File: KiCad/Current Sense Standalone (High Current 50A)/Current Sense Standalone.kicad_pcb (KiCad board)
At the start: 2 copper layers, 62.3 x 24.3 mm, 9 parts, among them J1 PLUG INPUT BATTERY IN HERE (X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, J3 V+/- TEST Header PIN, J6 to MCU GPIO PIN, J7 PLUG BATTERY OUTPUT HERE (XT6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, U1 INA139QPWRQ1

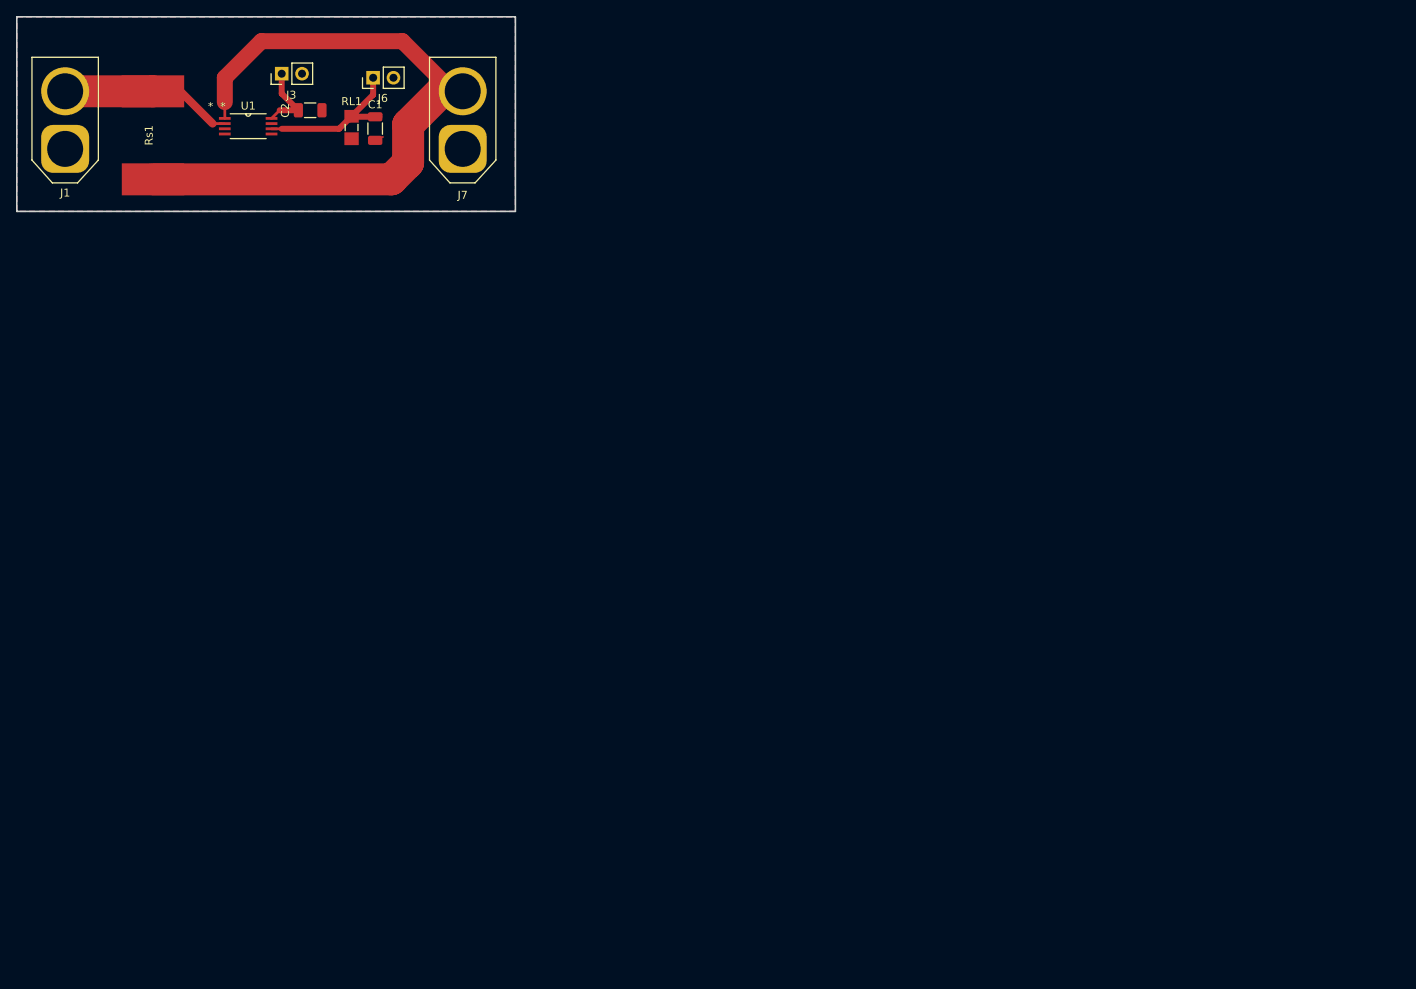
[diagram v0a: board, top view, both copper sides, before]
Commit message: Current Sense Dimensions
Adjusted dimensions of the width and length of the board. Still in-progress with the components.
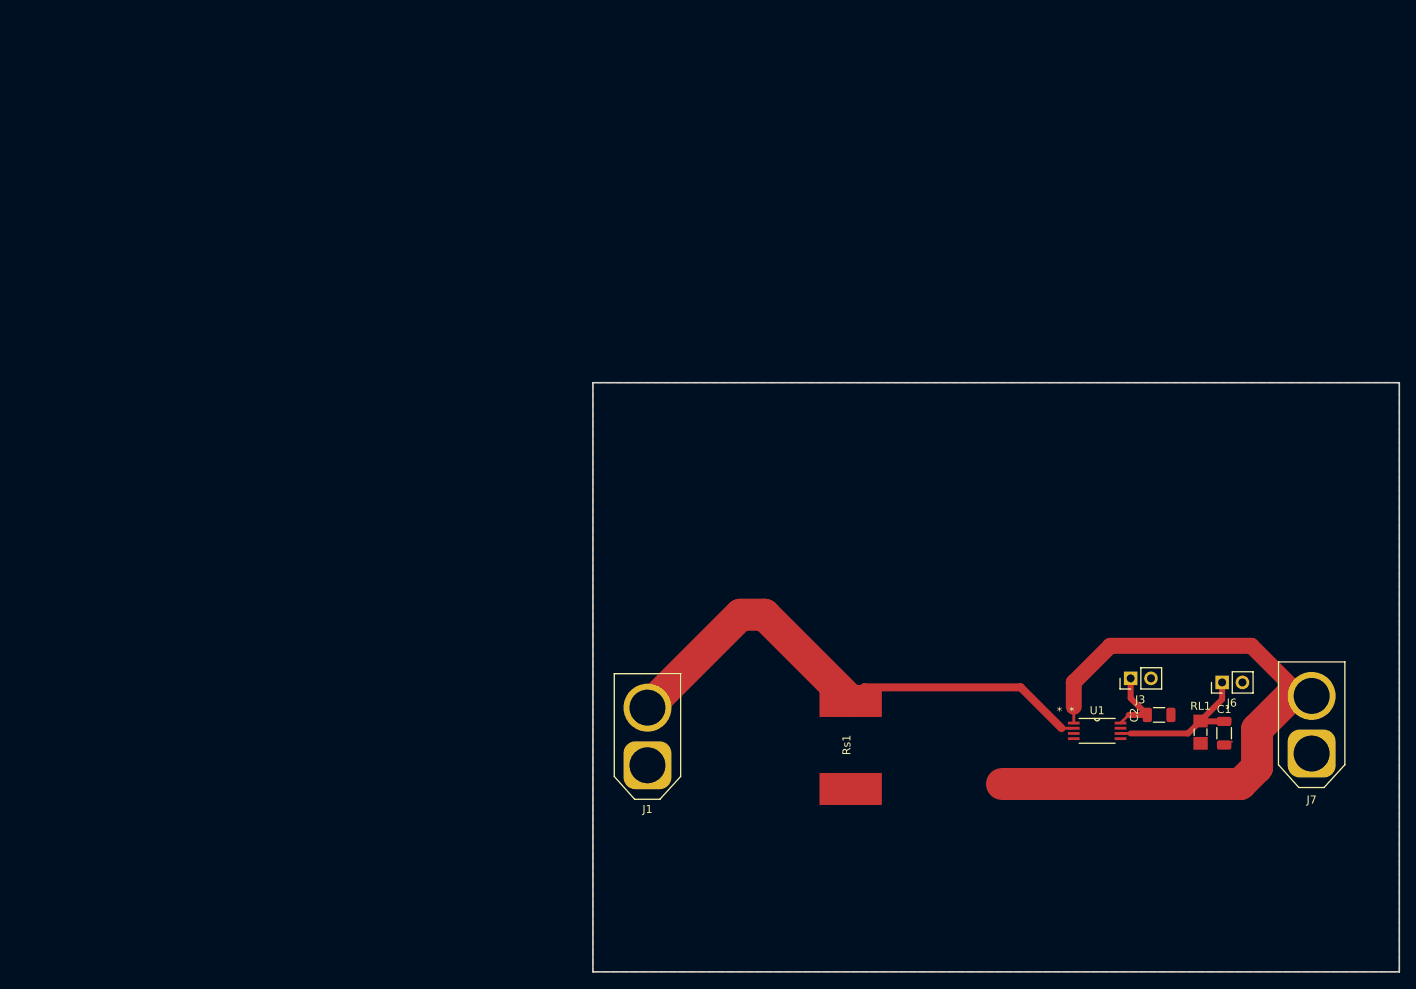
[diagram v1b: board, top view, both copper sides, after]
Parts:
- moved J3 130.3 mm to (151.8, 95.4)
- moved J6 130.3 mm to (163.3, 95.9)
- moved J7 130.3 mm to (174.5, 104.8)
- moved RL1 130.3 mm to (160.6, 102.1)
- moved C1 130.3 mm to (163.5, 102.3)
- moved C2 130.3 mm to (155.4, 100.0)
- moved U1 130.3 mm to (147.6, 102.0)
- moved Rs1 115.8 mm to (116.8, 103.7)
- moved J1 106.0 mm to (91.4, 106.3)
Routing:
- net /Batt+: track 27.3 -> 65.4 mm
- net GND: track 3.51 -> 0.88 mm
- removed copper zone on B.Cu, net GND
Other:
- board size 62.3 x 24.3 mm -> 100.8 x 73.6 mm

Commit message: Update Current Sense Standalone.kicad_pcb
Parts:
- moved J3 32.8 mm to (137.2, 66.0)
- moved J6 22.3 mm to (162.6, 73.7)
- moved U1 18.8 mm to (137.2, 86.4)
- moved Rs1 9.66 mm to (114.3, 94.4)
- moved J1 8.68 mm to (91.4, 97.6)
- moved J7 7.21 mm to (174.5, 97.6)
- moved C2 5.77 mm to (149.9, 101.6)
- moved RL1 3.14 mm to (157.5, 101.6)
- moved C1 0.65 mm to (163.5, 101.6)
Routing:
- net /Batt-: track 84.1 -> 0.00 mm
- net /Batt+: track 65.4 -> 0.00 mm
- net /Vout: track 21.1 -> 0.00 mm
- net /V-: track 9.21 -> 0.00 mm
- net GND: track 0.88 -> 0.00 mm
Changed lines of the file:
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@@
   (net 8 "/Batt-")
   (footprint "Mechatronic Footprints:AMASS_XT60-F_1x02_P7.20mm_Vertical" (layer "F.Cu")
-    (at 174.464045 104.790486 90)
+    (at 174.464045 97.58 90)
     (descr "AMASS female XT60, through hole, vertical, https://www.tme.eu/Document/2d152ced3b7a446066e6c419d84bb460/XT60%20SPEC.pdf")
     (tags "XT60 female vertical")
@@
   )
   (footprint "Capacitor_SMD:C_1206_3216Metric" (layer "F.Cu")
-    (at 155.396 99.964486)
+    (at 149.86 101.6)
     (descr "Capacitor SMD 1206 (3216 Metric), square (rectangular) end terminal, IPC_7351 nominal, (Body size source: IPC-SM-782 page 76, https://www.pcb-3d.com/wordpress/wp-content/uploads/ipc-sm-782a_amendment_1_and_2.pdf), generated with kicad-footprint-generator")
     (tags "capacitor")
@@
   )
   (footprint "RC1206FR-13100KL:RESC3216X65" (layer "F.Cu")
-    (at 160.573375 102.120486 -90)
+    (at 157.48 101.6 -90)
     (descr "<b>RESISTOR</b>")
     (property "Sheetfile" "Current Sense Standalone.kicad_sch")
@@
   )
   (footprint "Mechatronic Footprints:CSS2H-5930R" (layer "F.Cu")
-    (at 116.84 103.72 90)
+    (at 114.3 94.4 90)
     (property "Sheetfile" "Current Sense Standalone.kicad_sch")
     (property "Sheetname" "")
@@
   )
   (footprint "Capacitor_SMD:C_1206_3216Metric" (layer "F.Cu")
-    (at 163.524 102.250486 -90)
+    (at 163.524 101.6 -90)
     (descr "Capacitor SMD 1206 (3216 Metric), square (rectangular) end terminal, IPC_7351 nominal, (Body size source: IPC-SM-782 page 76, https://www.pcb-3d.com/wordpress/wp-content/uploads/ipc-sm-782a_amendment_1_and_2.pdf), generated with kicad-footprint-generator")
     (tags "capacitor")
@@
   )
   (footprint "Connector_PinHeader_2.54mm:PinHeader_1x02_P2.54mm_Vertical" (layer "F.Cu")
-    (at 151.84 95.392486 90)
+    (at 137.16 66.04 90)
     (descr "Through hole straight pin header, 1x02, 2.54mm pitch, single row")
     (tags "Through hole pin header THT 1x02 2.54mm single row")
@@
   )
   (footprint "Mechatronic Footprints:INA139_PW8" (layer "F.Cu")
-    (at 147.649 101.955485)
+    (at 137.16 86.36)
     (tags "INA139QPWRQ1 ")
     (property "Sheetfile" "Current Sense Standalone.kicad_sch")
@@
   )
   (footprint "Mechatronic Footprints:AMASS_XT60-M_1x02_P7.20mm_Vertical" (layer "F.Cu")
-    (at 91.44 106.26 90)
+    (at 91.44 97.58 90)
     (descr "AMASS female XT60, through hole, vertical, https://www.tme.eu/Document/2d152ced3b7a446066e6c419d84bb460/XT60%20SPEC.pdf")
     (tags "XT60 female vertical")
@@
   )
   (footprint "Connector_PinHeader_2.54mm:PinHeader_1x02_P2.54mm_Vertical" (layer "F.Cu")
-    (at 163.27 95.900486 90)
+    (at 162.56 73.66 90)
     (descr "Through hole straight pin header, 1x02, 2.54mm pitch, single row")
     (tags "Through hole pin header THT 1x02 2.54mm single row")
@@
   (gr_rect (start 84.62 58.44) (end 185.42 132.08)
     (stroke (width 0.2) (type default)) (fill none) (layer "Edge.Cuts"))
-  (segment (start 163.27 95.900486) (end 163.27 98.023861) (width 0.75) (layer "F.Cu") (net 1))
-  (segment (start 163.27 98.023861) (end 160.783751 100.51011) (width 0.75) (layer "F.Cu") (net 1))
-  (segment (start 160.783751 100.51011) (end 160.573375 100.51011) (width 0.25) (layer "F.Cu") (net 1))
-  (segment (start 164.062862 100.775486) (end 164.328238 100.51011) (width 0.25) (layer "F.Cu") (net 1))
-  (segment (start 160.838751 100.775486) (end 164.062862 100.775486) (width 0.75) (layer "F.Cu") (net 1))
-  (segment (start 150.57 102.280486) (end 151.84 102.280486) (width 0.35) (layer "F.Cu") (net 1))
-  (segment (start 151.84 102.280486) (end 159.013375 102.280486) (width 0.75) (layer "F.Cu") (net 1))
-  (segment (start 159.013375 102.280486) (end 160.573375 100.720486) (width 0.75) (layer "F.Cu") (net 1))
-  (segment (start 160.102999 100.980486) (end 160.573375 100.51011) (width 0.25) (layer "F.Cu") (net 1))
-  (segment (start 160.573375 100.51011) (end 160.838751 100.775486) (width 0.25) (layer "F.Cu") (net 1))
-  (segment (start 164.483078 103.30527) (end 164.478238 103.31011) (width 0.25) (layer "F.Cu") (net 2))
-  (segment (start 160.783751 103.31011) (end 160.163375 103.930486) (width 0.25) (layer "F.Cu") (net 2))
-  (segment (start 150.57 100.980486) (end 151.586 99.964486) (width 0.35) (layer "F.Cu") (net 3))
-  (segment (start 151.84 97.883486) (end 151.84 95.392486) (width 0.75) (layer "F.Cu") (net 3))
-  (segment (start 153.921 99.964486) (end 151.84 97.883486) (width 0.75) (layer "F.Cu") (net 3))
-  (segment (start 151.586 99.964486) (end 153.921 99.964486) (width 0.75) (layer "F.Cu") (net 3))
-  (segment (start 118.54 96.52) (end 138.093516 96.52) (width 1) (layer "F.Cu") (net 7))
-  (segment (start 144.22 101.630484) (end 144.728 101.630484) (width 0.25) (layer "F.Cu") (net 7))
-  (segment (start 103.061503 87.438497) (end 91.44 99.06) (width 4) (layer "F.Cu") (net 7))
-  (segment (start 143.204 101.630484) (end 144.22 101.630484) (width 0.35) (layer "F.Cu") (net 7))
-  (segment (start 138.093516 96.52) (end 143.204 101.630484) (width 1) (layer "F.Cu") (net 7))
-  (segment (start 116.84 98.22) (end 118.54 96.52) (width 1) (layer "F.Cu") (net 7))
-  (segment (start 116.84 98.22) (end 106.058497 87.438497) (width 4) (layer "F.Cu") (net 7))
-  (segment (start 106.058497 87.438497) (end 103.061503 87.438497) (width 4) (layer "F.Cu") (net 7))
-  (segment (start 171.813027 97.590486) (end 174.464045 97.590486) (width 4) (layer "F.Cu") (net 8))
-  (segment (start 167.64 101.763513) (end 171.813027 97.590486) (width 4) (layer "F.Cu") (net 8))
-  (segment (start 144.728 95.900486) (end 149.3 91.328486) (width 2) (layer "F.Cu") (net 8))
-  (segment (start 166.932045 91.328486) (end 173.194045 97.590486) (width 2) (layer "F.Cu") (net 8))
-  (segment (start 144.728 98.948486) (end 144.728 100.980486) (width 0.35) (layer "F.Cu") (net 8))
-  (segment (start 135.749273 108.598497) (end 135.751262 108.600486) (width 2) (layer "F.Cu") (net 8))
-  (segment (start 165.556 108.600486) (end 167.64 106.516486) (width 4) (layer "F.Cu") (net 8))
-  (segment (start 135.751262 108.600486) (end 165.556 108.600486) (width 4) (layer "F.Cu") (net 8))
-  (segment (start 144.728 98.948486) (end 144.728 95.900486) (width 2) (layer "F.Cu") (net 8))
-  (segment (start 149.3 91.328486) (end 166.932045 91.328486) (width 2) (layer "F.Cu") (net 8))
-  (segment (start 167.64 106.516486) (end 167.64 101.763513) (width 4) (layer "F.Cu") (net 8))
   (zone (net 2) (net_name "GND") (layer "F.Cu") (hatch edge 0.5)
     (connect_pads (clearance 0.5))

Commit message: Resume Builder - Jaxon
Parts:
- moved J3 48.9 mm to (160.0, 109.2)
- moved J6 39.8 mm to (144.8, 109.2)
- moved C2 23.1 mm to (162.6, 120.9), turned to -90 degrees
- moved C1 21.0 mm to (155.0, 120.8)
- moved RL1 21.0 mm to (149.0, 120.8)
- moved Rs1 20.1 mm to (132.7, 86.4), turned to 180 degrees
- moved J7 19.9 mm to (154.6, 97.5)
- moved J1 16.6 mm to (108.0, 97.4)
- moved U1 13.0 mm to (134.2, 99.1)
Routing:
- net /V-: track 0.00 -> 38.7 mm
- net /Vout: track 0.00 -> 31.5 mm
- net /Batt+: track 0.00 -> 14.6 mm
- net /Batt-: track 0.00 -> 14.6 mm
- added copper zone on F.Cu, net /Batt+
- added copper zone on F.Cu, net /Batt-
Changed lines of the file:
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@@
   (net 8 "/Batt-")
   (footprint "Mechatronic Footprints:AMASS_XT60-F_1x02_P7.20mm_Vertical" (layer "F.Cu")
-    (at 174.464045 97.58 90)
+    (at 154.558994 97.461689 90)
     (descr "AMASS female XT60, through hole, vertical, https://www.tme.eu/Document/2d152ced3b7a446066e6c419d84bb460/XT60%20SPEC.pdf")
     (tags "XT60 female vertical")
@@
   )
   (footprint "Capacitor_SMD:C_1206_3216Metric" (layer "F.Cu")
-    (at 149.86 101.6)
+    (at 162.56 120.855 -90)
     (descr "Capacitor SMD 1206 (3216 Metric), square (rectangular) end terminal, IPC_7351 nominal, (Body size source: IPC-SM-782 page 76, https://www.pcb-3d.com/wordpress/wp-content/uploads/ipc-sm-782a_amendment_1_and_2.pdf), generated with kicad-footprint-generator")
     (tags "capacitor")
@@
     (property "ki_keywords" "capacitor cap")
     (attr smd)
-    (fp_text reference "C2" (at -3.112128 0.016213 90) (layer "F.SilkS")
-        (effects (font (size 1 1) (thickness 0.15)))
-    )
-    (fp_text value "0.1uF" (at 3.158882 0.112988 90) (layer "F.Fab")
-        (effects (font (size 1 1) (thickness 0.15)))
-    )
-    (fp_text user "${REFERENCE}" (at 0 0) (layer "F.Fab")
+    (fp_text reference "C2" (at -3.112128 0.016213) (layer "F.SilkS")
+        (effects (font (size 1 1) (thickness 0.15)))
+    )
+    (fp_text value "0.1uF" (at 3.158882 0.112988) (layer "F.Fab")
+        (effects (font (size 1 1) (thickness 0.15)))
+    )
+    (fp_text user "${REFERENCE}" (at 0 0 90) (layer "F.Fab")
         (effects (font (size 0.8 0.8) (thickness 0.12)))
     )
@@
     (fp_line (start 1.6 0.8) (end -1.6 0.8)
       (stroke (width 0.1) (type solid)) (layer "F.Fab"))
-    (pad "1" smd roundrect (at -1.475 0) (size 1.15 1.8) (layers "F.Cu" "F.Paste" "F.Mask") (roundrect_rratio 0.2173913043)
+    (pad "1" smd roundrect (at -1.475 0 270) (size 1.15 1.8) (layers "F.Cu" "F.Paste" "F.Mask") (roundrect_rratio 0.2173913043)
       (net 3 "/V-") (pintype "passive"))
-    (pad "2" smd roundrect (at 1.475 0) (size 1.15 1.8) (layers "F.Cu" "F.Paste" "F.Mask") (roundrect_rratio 0.2173913043)
+    (pad "2" smd roundrect (at 1.475 0 270) (size 1.15 1.8) (layers "F.Cu" "F.Paste" "F.Mask") (roundrect_rratio 0.2173913043)
       (net 2 "GND") (pintype "passive"))
     (model "${KICAD6_3DMODEL_DIR}/Capacitor_SMD.3dshapes/C_1206_3216Metric.wrl"
@@
   )
   (footprint "RC1206FR-13100KL:RESC3216X65" (layer "F.Cu")
-    (at 157.48 101.6 -90)
+    (at 148.971 120.78 -90)
     (descr "<b>RESISTOR</b>")
     (property "Sheetfile" "Current Sense Standalone.kicad_sch")
@@
   )
   (footprint "Mechatronic Footprints:CSS2H-5930R" (layer "F.Cu")
-    (at 114.3 94.4 90)
+    (at 132.72 86.36 180)
     (property "Sheetfile" "Current Sense Standalone.kicad_sch")
     (property "Sheetname" "")
@@
     (property "ki_keywords" "r resistor")
     (attr smd)
-    (fp_text reference "Rs1" (at 0 -0.5 90 unlocked) (layer "F.SilkS")
-        (effects (font (size 1 1) (thickness 0.15)))
-    )
-    (fp_text value "R_Small_US" (at 0 -5.08 90 unlocked) (layer "F.Fab")
-        (effects (font (size 1 1) (thickness 0.15)))
-    )
-    (fp_text user "${REFERENCE}" (at 0 4.953 90 unlocked) (layer "F.Fab")
-        (effects (font (size 1 1) (thickness 0.15)))
-    )
-    (pad "1" smd rect (at -5.5 0 180) (size 7.8 4) (layers "F.Cu" "F.Paste" "F.Mask")
+    (fp_text reference "Rs1" (at 0 -0.5 unlocked) (layer "F.SilkS")
+        (effects (font (size 1 1) (thickness 0.15)))
+    )
+    (fp_text value "R_Small_US" (at 0 -5.08 unlocked) (layer "F.Fab")
+        (effects (font (size 1 1) (thickness 0.15)))
+    )
+    (fp_text user "${REFERENCE}" (at 0 4.953 unlocked) (layer "F.Fab")
+        (effects (font (size 1 1) (thickness 0.15)))
+    )
+    (pad "1" smd rect (at -5.5 0 270) (size 7.8 4) (layers "F.Cu" "F.Paste" "F.Mask")
       (net 8 "/Batt-") (pintype "passive") (thermal_bridge_angle 45))
-    (pad "2" smd rect (at 5.5 0 180) (size 7.8 4) (layers "F.Cu" "F.Paste" "F.Mask")
+    (pad "2" smd rect (at 5.5 0 270) (size 7.8 4) (layers "F.Cu" "F.Paste" "F.Mask")
       (net 7 "/Batt+") (pintype "passive") (thermal_bridge_angle 45))
   )
   (footprint "Capacitor_SMD:C_1206_3216Metric" (layer "F.Cu")
-    (at 163.524 101.6 -90)
+    (at 155.015 120.78 -90)
     (descr "Capacitor SMD 1206 (3216 Metric), square (rectangular) end terminal, IPC_7351 nominal, (Body size source: IPC-SM-782 page 76, https://www.pcb-3d.com/wordpress/wp-content/uploads/ipc-sm-782a_amendment_1_and_2.pdf), generated with kicad-footprint-generator")
     (tags "capacitor")
@@
   )
   (footprint "Connector_PinHeader_2.54mm:PinHeader_1x02_P2.54mm_Vertical" (layer "F.Cu")
-    (at 137.16 66.04 90)
+    (at 160.02 109.22 90)
     (descr "Through hole straight pin header, 1x02, 2.54mm pitch, single row")
     (tags "Through hole pin header THT 1x02 2.54mm single row")
@@
   )
   (footprint "Mechatronic Footprints:INA139_PW8" (layer "F.Cu")
-    (at 137.16 86.36)
+    (at 134.239 99.06)
     (tags "INA139QPWRQ1 ")
     (property "Sheetfile" "Current Sense Standalone.kicad_sch")
@@
   )
   (footprint "Mechatronic Footprints:AMASS_XT60-M_1x02_P7.20mm_Vertical" (layer "F.Cu")
-    (at 91.44 97.58 90)
+    (at 108.024461 97.415276 90)
     (descr "AMASS female XT60, through hole, vertical, https://www.tme.eu/Document/2d152ced3b7a446066e6c419d84bb460/XT60%20SPEC.pdf")
     (tags "XT60 female vertical")
@@
   )
   (footprint "Connector_PinHeader_2.54mm:PinHeader_1x02_P2.54mm_Vertical" (layer "F.Cu")
-    (at 162.56 73.66 90)
+    (at 144.78 109.22 90)
     (descr "Through hole straight pin header, 1x02, 2.54mm pitch, single row")
     (tags "Through hole pin header THT 1x02 2.54mm single row")
@@
   (gr_rect (start 84.62 58.44) (end 185.42 132.08)
     (stroke (width 0.2) (type default)) (fill none) (layer "Edge.Cuts"))
+  (segment (start 144.78 109.22) (end 144.78 115.189) (width 0.25) (layer "F.Cu") (net 1))
+  (segment (start 144.78 109.22) (end 144.78 106.090599) (width 0.25) (layer "F.Cu") (net 1))
+  (segment (start 144.78 106.090599) (end 138.074402 99.385001) (width 0.25) (layer "F.Cu") (net 1))
+  (segment (start 138.074402 99.385001) (end 137.16 99.385001) (width 0.25) (layer "F.Cu") (net 1))
+  (segment (start 144.78 115.189) (end 148.971 119.38) (width 0.25) (layer "F.Cu") (net 1))
+  (segment (start 155.015 119.305) (end 154.94 119.38) (width 0.25) (layer "F.Cu") (net 1))
+  (segment (start 154.94 119.38) (end 148.971 119.38) (width 0.25) (layer "F.Cu") (net 1))
+  (segment (start 160.02 109.22) (end 156.21 109.22) (width 0.25) (layer "F.Cu") (net 3))
+  (segment (start 160.02 109.22) (end 160.02 116.84) (width 0.25) (layer "F.Cu") (net 3))
+  (segment (start 160.02 116.84) (end 162.56 119.38) (width 0.25) (layer "F.Cu") (net 3))
+  (segment (start 156.21 109.22) (end 145.075001 98.085001) (width 0.25) (layer "F.Cu") (net 3))
+  (segment (start 145.075001 98.085001) (end 137.16 98.085001) (width 0.25) (layer "F.Cu") (net 3))
+  (segment (start 130.3814 98.734999) (end 127.22 95.573599) (width 0.2) (layer "F.Cu") (net 7))
+  (segment (start 127.22 95.573599) (end 127.22 86.36) (width 0.2) (layer "F.Cu") (net 7))
+  (segment (start 131.318 98.734999) (end 130.3814 98.734999) (width 0.2) (layer "F.Cu") (net 7))
+  (segment (start 138.22 91.183001) (end 138.22 86.36) (width 0.2) (layer "F.Cu") (net 8))
+  (segment (start 131.318 98.085001) (end 138.22 91.183001) (width 0.2) (layer "F.Cu") (net 8))
+  (zone (net 7) (net_name "/Batt+") (layer "F.Cu") (hatch edge 0.5)
+    (priority 1)
+    (connect_pads (clearance 0.5))
+    (min_thickness 0.25) (filled_areas_thickness no)
+    (fill yes (thermal_gap 0.5) (thermal_bridge_width 0.5))
+    (polygon
+      (pts
+        (xy 89.96 63.5)
+        (xy 89.96 93.98)
+        (xy 133.14 93.98)
+        (xy 133.14 63.5)
+      )
+    )
+  )
   (zone (net 2) (net_name "GND") (layer "F.Cu") (hatch edge 0.5)
     (connect_pads (clearance 0.5))
@@
       )
     )
+  )
+  (zone (net 8) (net_name "/Batt-") (layer "F.Cu") (hatch edge 0.5)
+    (priority 2)
+    (connect_pads (clearance 0.5))
+    (min_thickness 0.25) (filled_areas_thickness no)
+    (fill yes (thermal_gap 0.5) (thermal_bridge_width 0.5))
+    (polygon
+      (pts
+        (xy 134.62 63.5)
+        (xy 180.34 63.5)
+        (xy 180.34 93.98)
+        (xy 134.62 93.98)
+      )
+    )
